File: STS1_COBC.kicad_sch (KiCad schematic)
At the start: 14 parts, among them U1 coordinate_system

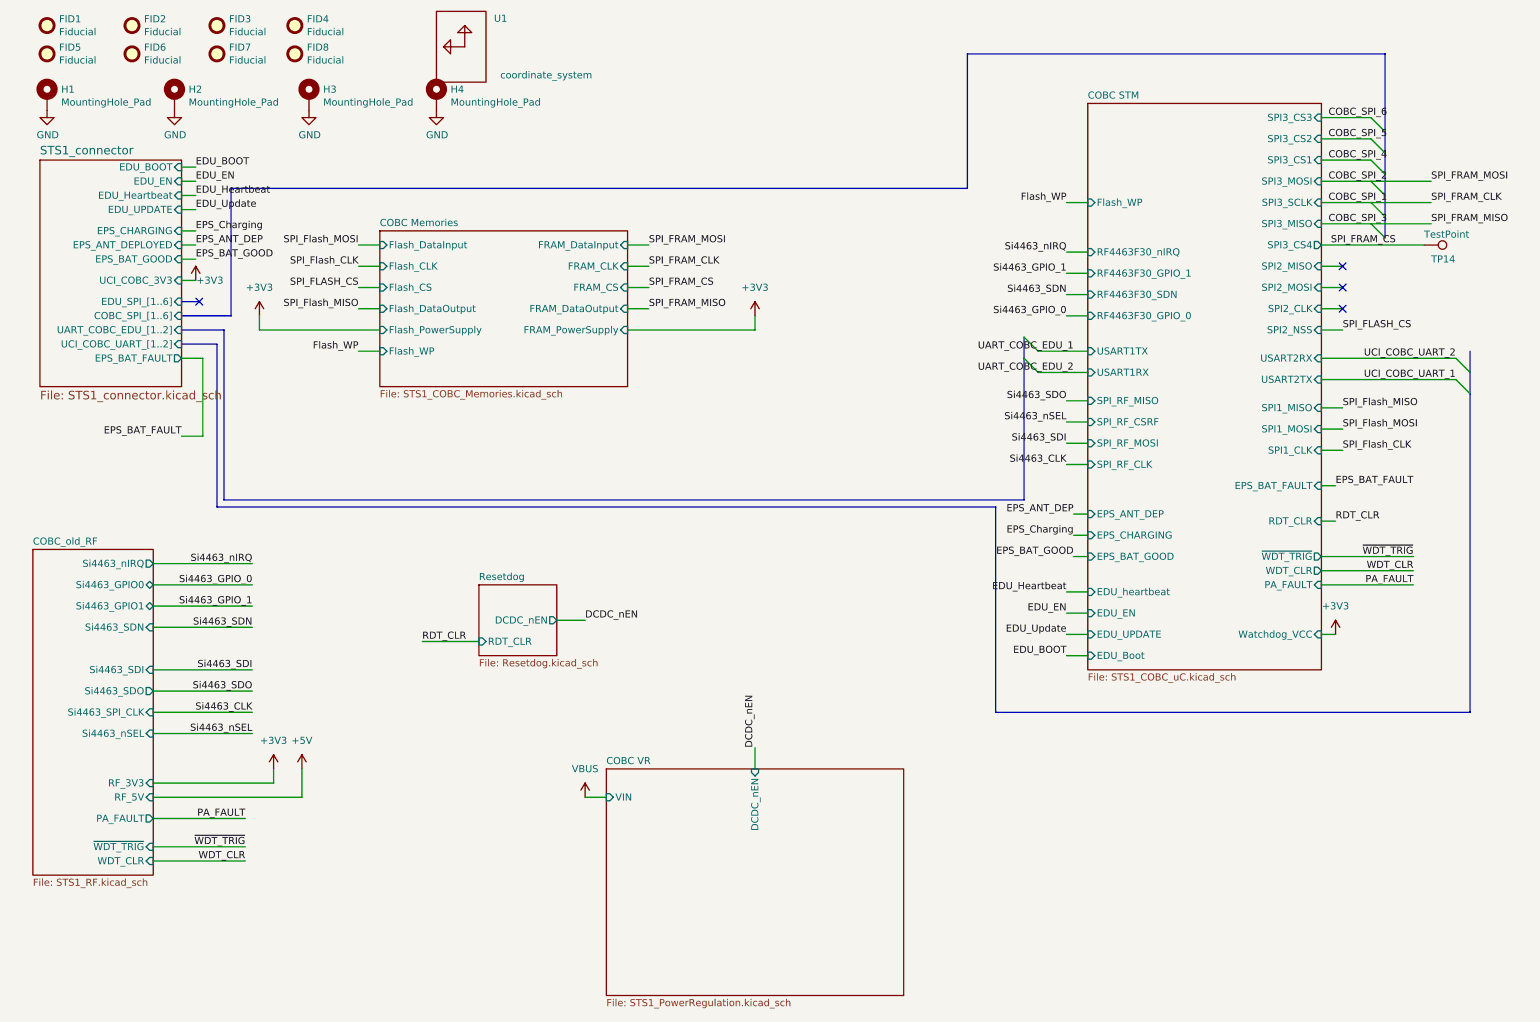
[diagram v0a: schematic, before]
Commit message: feat: clean up schematic
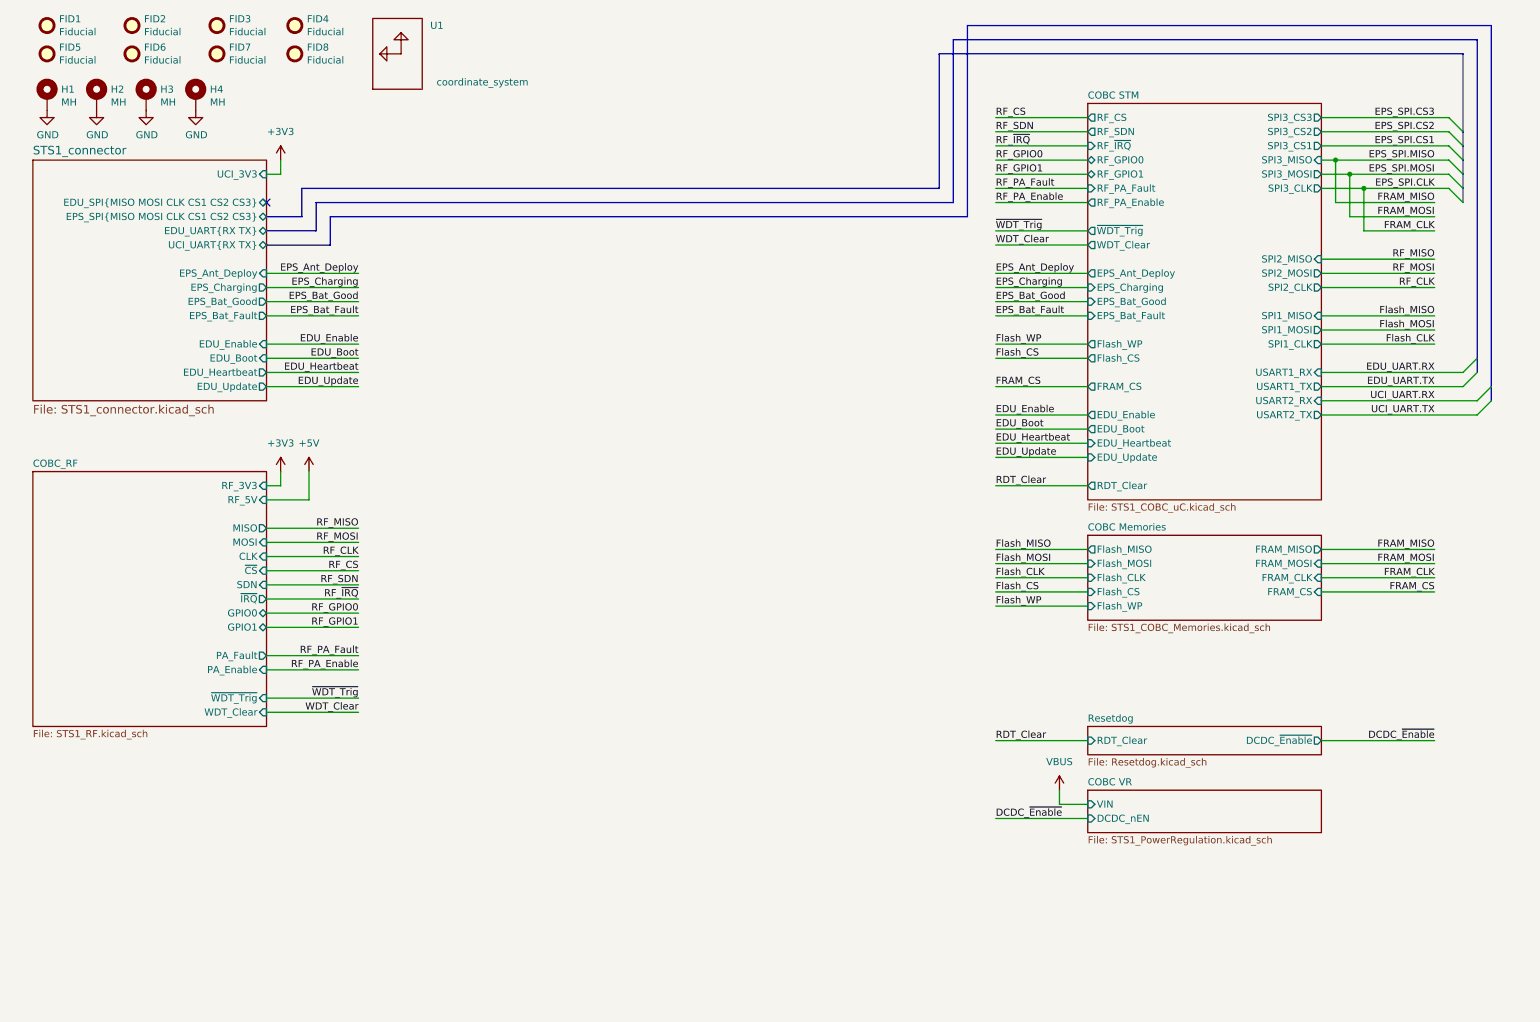
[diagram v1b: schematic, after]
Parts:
- removed TP14: TestPoint, STS1library:STS1_Testpoint, symbol Connector:TestPoint
- H1, H2, H3, H4: value MountingHole_Pad -> MH
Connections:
- no-connect marks 4 -> 1
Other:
- sheet COBC_old_RF renamed COBC_RF
- sheet COBC Memories ports: added FRAM_MISO, FRAM_MOSI, Flash_MISO, Flash_MOSI; removed FRAM_DataInput, FRAM_DataOutput, FRAM_PowerSupply, Flash_DataInput, Flash_DataOutput, Flash_PowerSupply
- sheet COBC STM ports: added EDU_Enable, EDU_Heartbeat, EDU_Update, EPS_Ant_Deploy, EPS_Bat_Fault, EPS_Bat_Good, EPS_Charging, FRAM_CS, Flash_CS, RDT_Clear, RF_CS, RF_GPIO0, RF_GPIO1, RF_PA_Enable, RF_PA_Fault, RF_SDN, RF_~{IRQ}, SPI3_CLK, USART1_RX, USART1_TX, USART2_RX, USART2_TX, WDT_Clear, ~{WDT_Trig}; removed EDU_EN, EDU_UPDATE, EDU_heartbeat, EPS_ANT_DEP, EPS_BAT_FAULT, EPS_BAT_GOOD, EPS_CHARGING, PA_FAULT, RDT_CLR, RF4463F30_GPIO_0, RF4463F30_GPIO_1, RF4463F30_SDN, RF4463F30_nIRQ, SPI2_NSS, SPI3_CS4, SPI3_SCLK, SPI_RF_CLK, SPI_RF_CSRF, SPI_RF_MISO, SPI_RF_MOSI, USART1RX, USART1TX, USART2RX, USART2TX, WDT_CLR, Watchdog_VCC, ~{WDT_TRIG}
- sheet COBC_RF ports: added CLK, GPIO0, GPIO1, MISO, MOSI, PA_Enable, PA_Fault, SDN, WDT_Clear, ~{CS}, ~{IRQ}, ~{WDT_Trig}; removed PA_FAULT, Si4463_GPIO0, Si4463_GPIO1, Si4463_SDI, Si4463_SDN, Si4463_SDO, Si4463_SPI_CLK, Si4463_nIRQ, Si4463_nSEL, WDT_CLR, ~{WDT_TRIG}
- sheet Resetdog ports: added DCDC_~{Enable}, RDT_Clear; removed DCDC_nEN, RDT_CLR
- sheet STS1_connector ports: added EDU_Boot, EDU_Enable, EDU_SPI{MISO MOSI CLK CS1 CS2 CS3}, EDU_UART{RX TX}, EDU_Update, EPS_Ant_Deploy, EPS_Bat_Fault, EPS_Bat_Good, EPS_Charging, EPS_SPI{MISO MOSI CLK CS1 CS2 CS3}, UCI_3V3, UCI_UART{RX TX}; removed COBC_SPI_[1..6], EDU_BOOT, EDU_EN, EDU_SPI_[1..6], EDU_UPDATE, EPS_ANT_DEPLOYED, EPS_BAT_FAULT, EPS_BAT_GOOD, EPS_CHARGING, UART_COBC_EDU_[1..2], UCI_COBC_3V3, UCI_COBC_UART_[1..2]
- moved on the sheet: H2, H3, H4, U1

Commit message: feat: more schematic cleanup
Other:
- sheet COBC Memories ports: added Flash_~{WP}; removed Flash_WP
- sheet COBC STM ports: added Flash_~{WP}; removed Flash_WP

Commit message: Fix footprint assignments: all IC should have U designator
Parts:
- renumbered U1 to CS1
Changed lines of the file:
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@@
   (symbol (lib_id "STS-connector:coordinate_system") (at 81.28 20.32 90) (unit 1)
     (in_bom yes) (on_board yes)
-    (property "Reference" "U1" (id 0) (at 88.9 15.24 90)
+    (property "Reference" "CS1" (id 0) (at 88.9 15.24 90)
       (effects (font (size 1.27 1.27)) (justify left))
     )
@@
       (reference "C83") (unit 1) (value "1n") (footprint "Capacitor_SMD:C_0603_1608Metric")
     )
+    (path "/00000000-0000-0000-0000-0000602f576d"
+      (reference "CS1") (unit 1) (value "coordinate_system") (footprint "STS_connector:Coordinates")
+    )
     (path "/00000000-0000-0000-0000-000059c45183/00000000-0000-0000-0000-00006179b797"
       (reference "CSBI_1") (unit 1) (value "~") (footprint "Connector_PinSocket_2.00mm:PinSocket_2x25_P2.00mm_Vertical")
@@
       (reference "FID8") (unit 1) (value "Fiducial") (footprint "Fiducial:Fiducial_0.75mm_Mask1.5mm")
     )
-    (path "/ac6659d3-0531-4d8c-b6db-7e3a6843f21e/00000000-0000-0000-0000-0000612a5631"
-      (reference "FLASH1") (unit 1) (value "W25Q01JVZEIQ") (footprint "STSLib:SON127P800X600X80-9N-D")
-    )
-    (path "/ac6659d3-0531-4d8c-b6db-7e3a6843f21e/00000000-0000-0000-0000-0000612a5f08"
-      (reference "FRAM1") (unit 1) (value "CY15B108QN-40SXI") (footprint "STSLib:SOIC127P800X203-8N")
-    )
     (path "/00000000-0000-0000-0000-0000602e546e"
       (reference "H1") (unit 1) (value "MH") (footprint "MountingHole:MountingHole_4.3mm_M4_Pad_Via")
@@
       (reference "H4") (unit 1) (value "MH") (footprint "MountingHole:MountingHole_4.3mm_M4_Pad_Via")
     )
-    (path "/be3cc363-80eb-4df5-9a1b-912085b5cf84/00000000-0000-0000-0000-000061674186"
-      (reference "IC2") (unit 1) (value "STWD100PYW83F") (footprint "SamacSys_Parts:SOT65P210X110-5N")
-    )
-    (path "/be3cc363-80eb-4df5-9a1b-912085b5cf84/00000000-0000-0000-0000-000061274132"
-      (reference "IC3") (unit 1) (value "STM32F411RET6TR") (footprint "STSLib:QFP50P1200X1200X160-64N")
-    )
     (path "/a8678e8a-595e-4c52-9d87-4220609965c5/00000000-0000-0000-0000-0000616a364e"
       (reference "J1") (unit 1) (value "UHF") (footprint "Connector_Coaxial:SMB_Jack_Vertical")
@@
       (reference "TP13") (unit 1) (value "3V3") (footprint "STS1library:STS1_Testpoint")
     )
-    (path "/00000000-0000-0000-0000-0000602f576d"
-      (reference "U1") (unit 1) (value "coordinate_system") (footprint "STS_connector:Coordinates")
+    (path "/ac6659d3-0531-4d8c-b6db-7e3a6843f21e/00000000-0000-0000-0000-0000612a5631"
+      (reference "U1") (unit 1) (value "W25Q01JVZEIQ") (footprint "STSLib:SON127P800X600X80-9N-D")
     )
     (path "/a8678e8a-595e-4c52-9d87-4220609965c5/8e389f53-343f-464a-adff-0fef404f38e7"
@@
       (reference "U16") (unit 1) (value "F2972") (footprint "lsf-kicad-lib:IDT_NEG-12-1EP_2x2mm_P0.5mm_EP1.1x1.1mm_ThermalVias")
     )
+    (path "/ac6659d3-0531-4d8c-b6db-7e3a6843f21e/00000000-0000-0000-0000-0000612a5f08"
+      (reference "U17") (unit 1) (value "CY15B108QN-40SXI") (footprint "STSLib:SOIC127P800X203-8N")
+    )
+    (path "/be3cc363-80eb-4df5-9a1b-912085b5cf84/00000000-0000-0000-0000-000061674186"
+      (reference "U18") (unit 1) (value "STWD100PYW83F") (footprint "SamacSys_Parts:SOT65P210X110-5N")
+    )
+    (path "/be3cc363-80eb-4df5-9a1b-912085b5cf84/00000000-0000-0000-0000-000061274132"
+      (reference "U19") (unit 1) (value "STM32F411RET6TR") (footprint "STSLib:QFP50P1200X1200X160-64N")
+    )
     (path "/be3cc363-80eb-4df5-9a1b-912085b5cf84/00000000-0000-0000-0000-00006254c1e3"
